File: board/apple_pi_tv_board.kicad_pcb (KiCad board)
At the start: 4 copper layers, 61 x 85.1 mm, 78 parts, among them J1 RJ45, J3 5-1775444-8, J4 JTAG_TC2030, J5 BM02B-ACHSS-GAN-TF, T1 H5007NL, U1 HDMI/USB, U11 TPD4EUSB30, U12 RT9742GGJ5, U2 apple tv tos link, U3 RPi_4, U4 RP2354A, U5 RT9742GGJ5, U6 TPD4EUSB30, U7 IRM-V838M3-C/TR1, U8 74LVC1G07, U9 TPS61232DRC, Y1 ABM8-272-T3

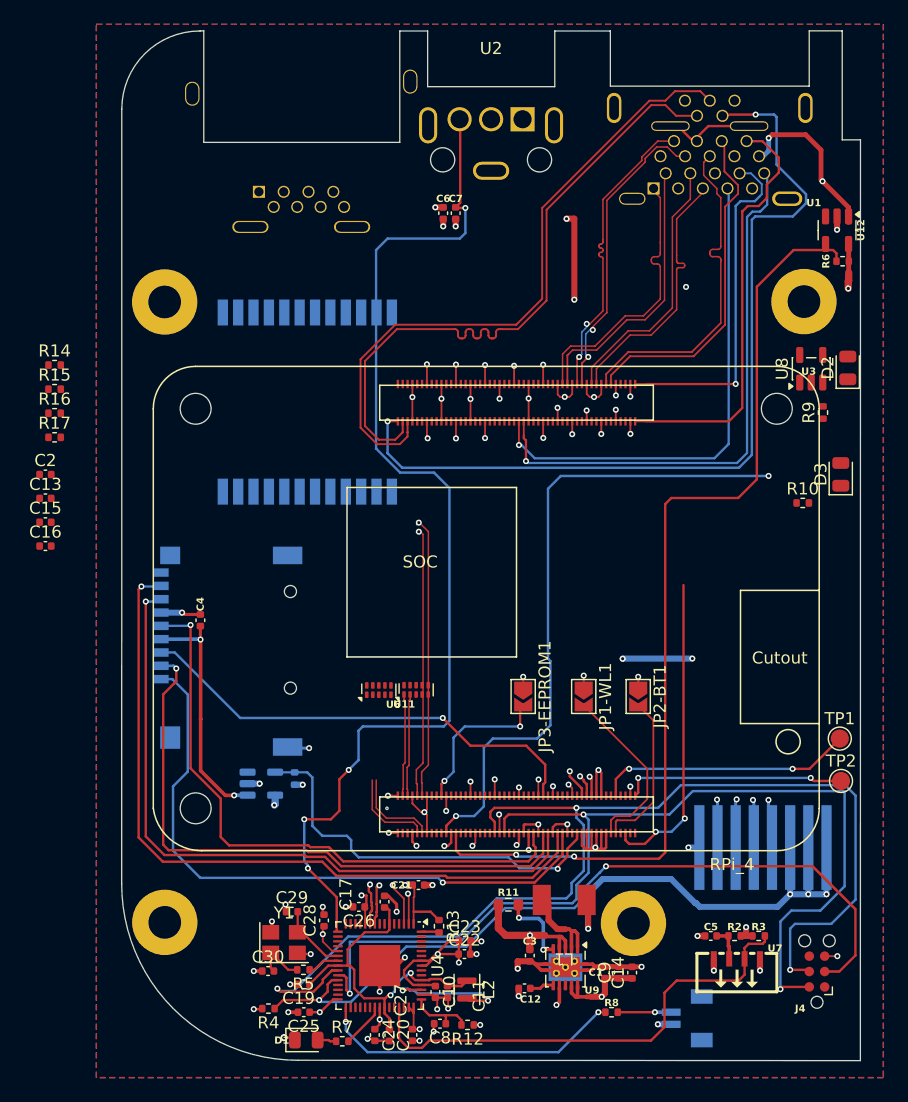
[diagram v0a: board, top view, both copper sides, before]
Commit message: got the ethernet routed
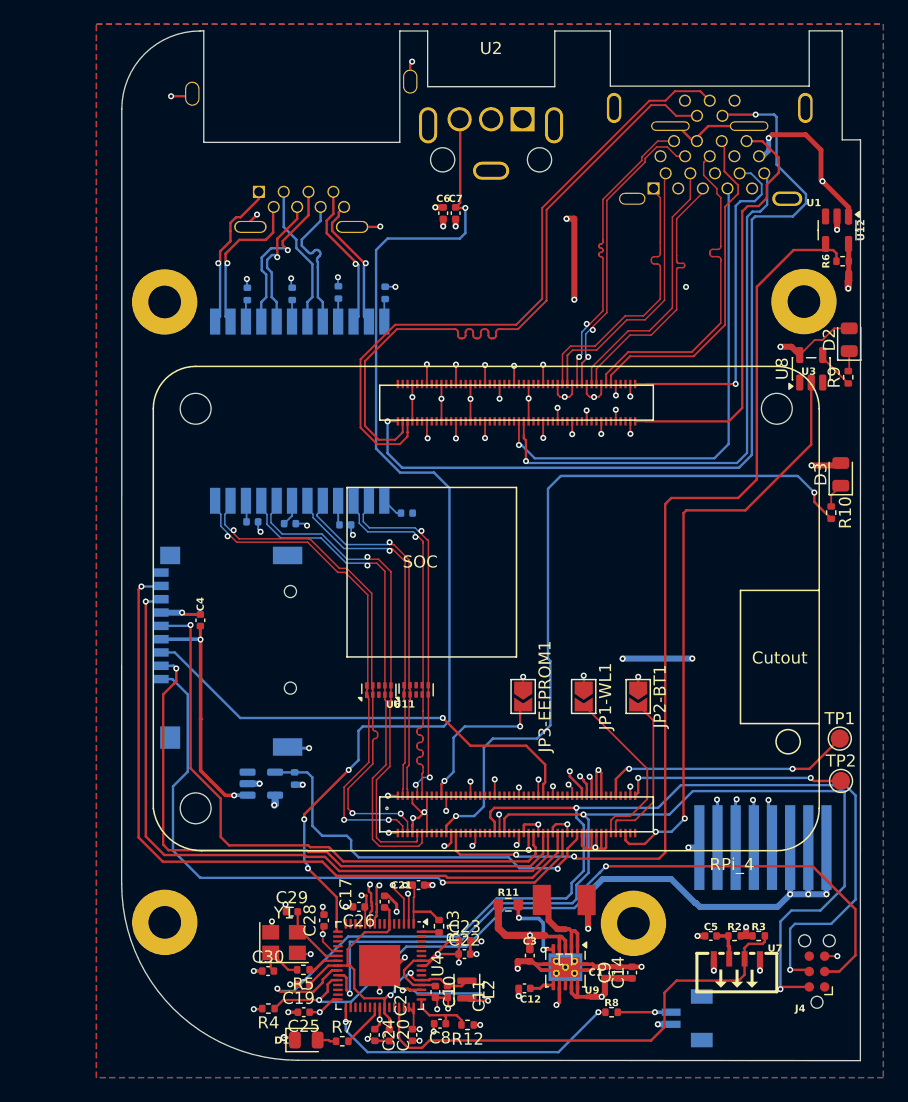
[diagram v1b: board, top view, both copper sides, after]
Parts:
- C13, C15, C16, C2: value C_Small -> 0.1uf; moved to B.Cu
- J1: value RJ45 -> RJ45_Shielded
- R14, R15, R16, R17: moved to B.Cu
- moved C16 30.0 mm to (101.6, 105.4), turned to 180 degrees
- moved R14 27.9 mm to (99.8, 87.2), turned to -90 degrees
- moved C2 25.1 mm to (96.6, 106.3), turned to 180 degrees
- moved R15 24.8 mm to (96.0, 87.2), turned to -90 degrees
- moved R16 22.0 mm to (92.2, 87.3), turned to -90 degrees
- moved C13 20.3 mm to (92.0, 106.2), turned to 180 degrees
- moved R17 19.8 mm to (88.5, 87.3), turned to -90 degrees
- moved C15 17.1 mm to (88.9, 106.1), turned to 180 degrees
- moved R9 3.58 mm to (138.1, 94.2)
- moved R10 2.48 mm to (136.7, 105.3), turned to -90 degrees
- moved D2 2.33 mm to (138.2, 91.1)
- moved T1 0.98 mm to (92.8, 97.0)
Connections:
- J1 pad 1: unconnected-(J1-Pad1) -> /HDMI_RJ45_USB/MX3_P
- J1 pad 2: unconnected-(J1-Pad2) -> /HDMI_RJ45_USB/MX3_N
- J1 pad 3: unconnected-(J1-Pad3) -> /HDMI_RJ45_USB/MX1_P
- J1 pad 4: unconnected-(J1-Pad4) -> /HDMI_RJ45_USB/MX2_N
- J1 pad 5: unconnected-(J1-Pad5) -> /HDMI_RJ45_USB/MX2_P
- J1 pad 6: unconnected-(J1-Pad6) -> /HDMI_RJ45_USB/MX1_N
- J1 pad 7: unconnected-(J1-Pad7) -> /HDMI_RJ45_USB/MX0_P
- J1 pad 8: unconnected-(J1-Pad8) -> /HDMI_RJ45_USB/MX0_N
- U11 pad 4: unconnected-(U11-D2+-Pad4) -> /TRD0_P
- U11 pad 5: unconnected-(U11-D2--Pad5) -> /TRD0_N
- U6 pad 1: /TRD3_N -> /TRD3_P
- U6 pad 2: /TRD3_P -> /TRD3_N
- U6 pad 4: /TRD2_N -> /TRD2_P
- U6 pad 5: /TRD2_P -> /TRD2_N
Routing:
- net /TRD3_N: track 0.00 -> 42.3 mm, vias 0 -> 3
- net /TRD3_P: track 0.00 -> 42.1 mm, vias 0 -> 3
- net /TRD2_P: track 7.29 -> 41.5 mm, vias 0 -> 1
- net /TRD2_N: track 7.30 -> 40.4 mm, vias 0 -> 1
- net +3V3: track 182.7 -> 208.6 mm, vias 20 -> 22
- net Net-(U3A-PI_LED_~{PWR}): track 25.9 -> 49.8 mm
- net /TRD1_P: track 8.48 -> 30.3 mm, vias 0 -> 1
- net /TRD1_N: track 8.48 -> 30.3 mm, vias 0 -> 1
- net GND: track 147.7 -> 162.0 mm, vias 84 -> 95
- net /HDMI_RJ45_USB/MX2_P: track 0.00 -> 14.0 mm, vias 0 -> 1
- net /HDMI_RJ45_USB/MX3_N: track 0.00 -> 12.7 mm, vias 0 -> 1
- net /HDMI_RJ45_USB/MX3_P: track 0.00 -> 12.6 mm, vias 0 -> 1
- net /HDMI_RJ45_USB/MX0_P: track 0.00 -> 12.3 mm, vias 0 -> 1
- net /HDMI_RJ45_USB/MX1_P: track 0.00 -> 11.9 mm
- net /HDMI_RJ45_USB/MX1_N: track 0.00 -> 11.8 mm
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
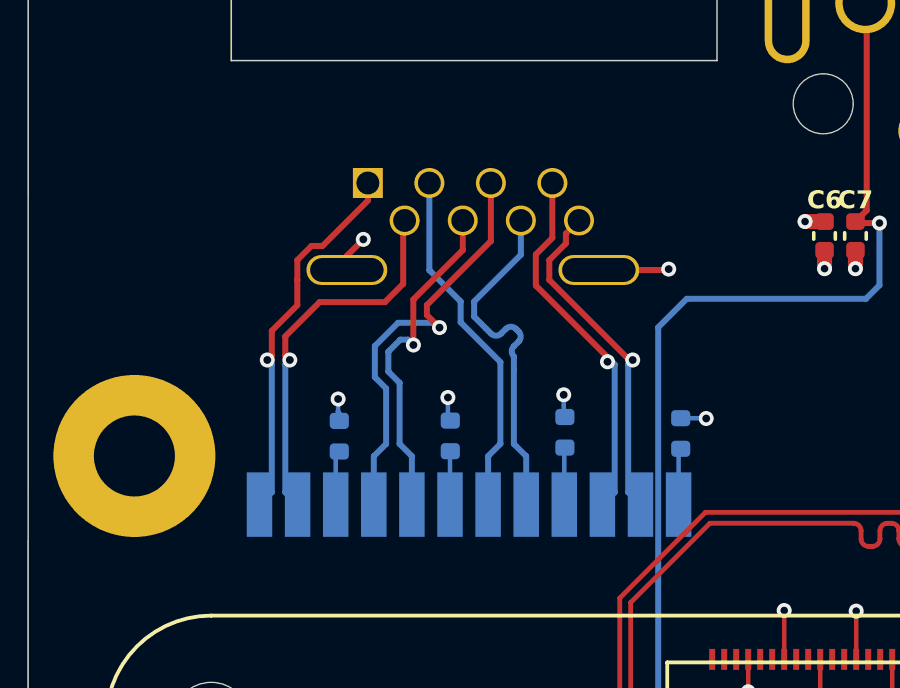
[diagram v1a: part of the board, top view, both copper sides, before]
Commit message: removed some via's
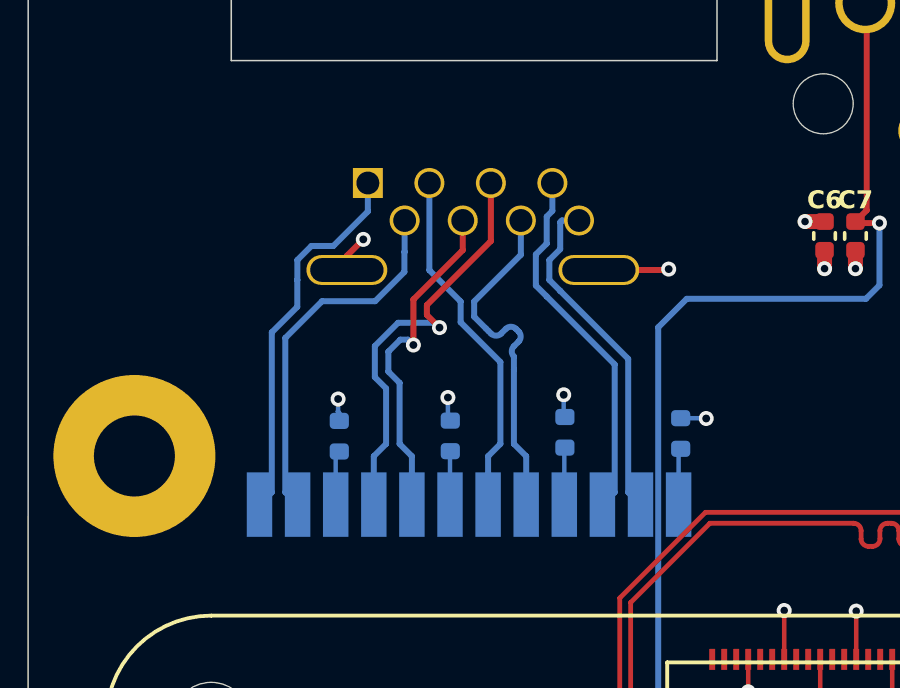
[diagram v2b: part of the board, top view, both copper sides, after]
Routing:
- net /HDMI_RJ45_USB/MX3_N: track 12.7 -> 12.4 mm, vias 1 -> 0
- net /HDMI_RJ45_USB/MX0_N: track 11.3 -> 11.5 mm, vias 1 -> 0
- net /HDMI_RJ45_USB/MX0_P: track 12.3 -> 12.2 mm, vias 1 -> 0
- net /HDMI_RJ45_USB/MX3_P: track 12.6 -> 12.7 mm, vias 1 -> 0

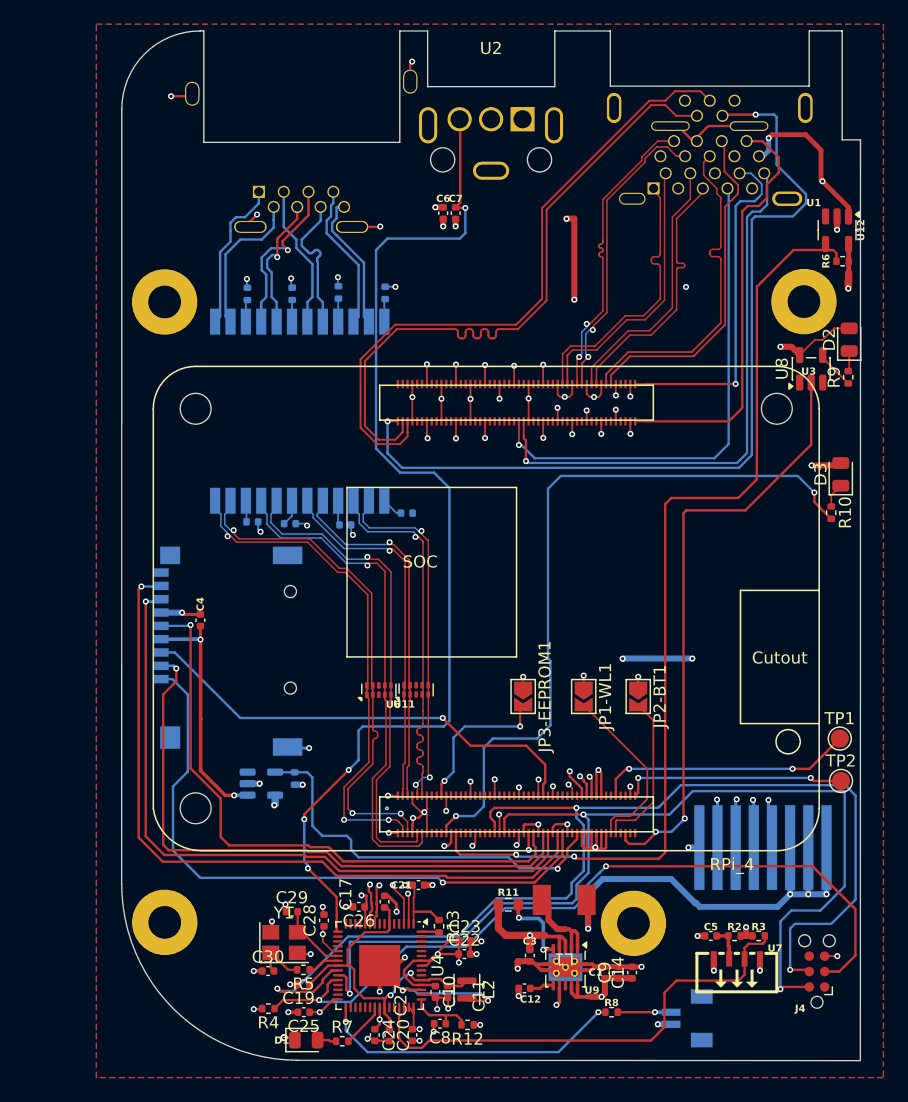
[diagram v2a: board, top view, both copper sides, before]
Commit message: made the cutout for the magnet isolater
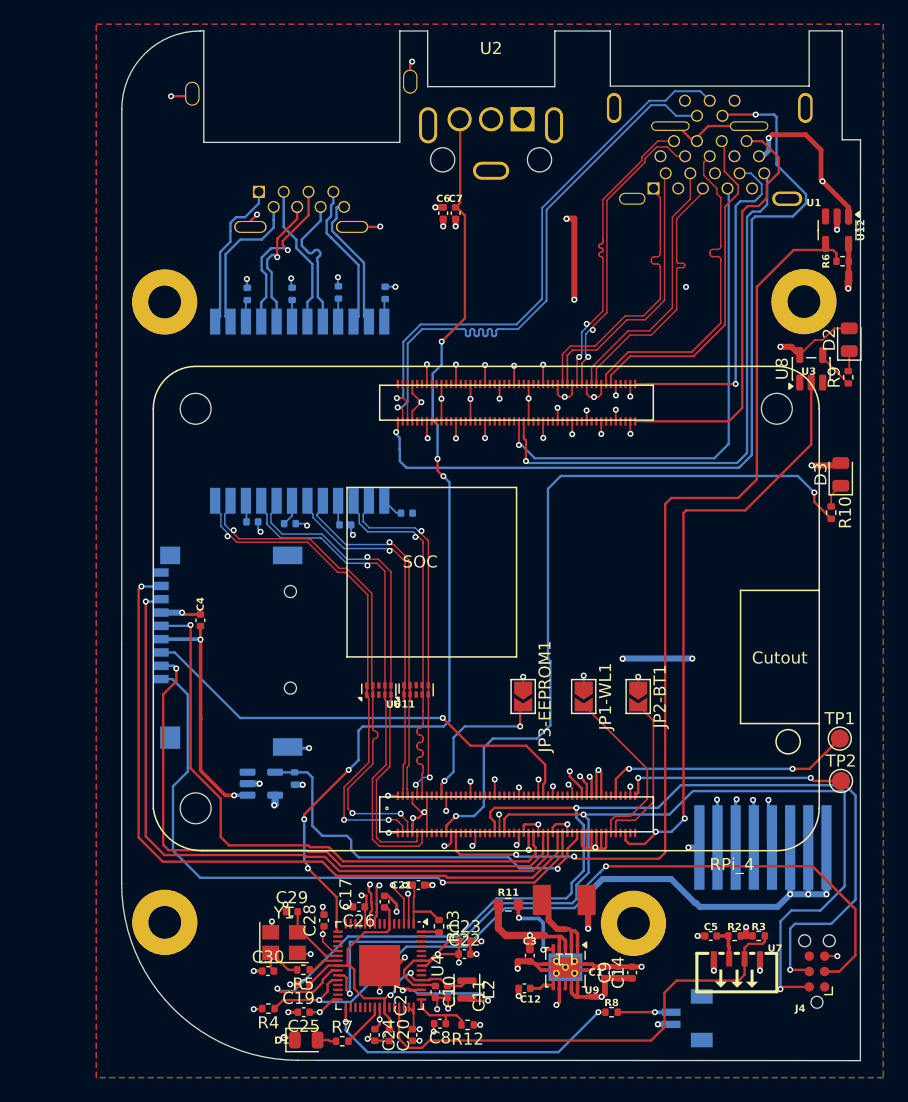
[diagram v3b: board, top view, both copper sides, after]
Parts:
- R10, R9: value R -> 1k
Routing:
- net /Pico_TOSLINK_IR/toslink: track 88.0 -> 78.6 mm, vias 4 -> 6
- net /USB_D+: track 54.4 -> 46.3 mm, vias 0 -> 1
- net /USB_D-: track 54.3 -> 47.7 mm, vias 0 -> 1
- net /USB_ID: track 71.5 -> 70.2 mm
- net GND: track 162.0 -> 162.6 mm

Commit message: should be the last build
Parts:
- moved J3 3.08 mm to (131.0, 134.5), turned to 180 degrees
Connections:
- J3 pad 1: GND -> /Power/power in
- J3 pad 2: GND -> /Power/power in
- J3 pad 3: GND -> /Power/power in
- J3 pad 6: /Power/power in -> GND
- J3 pad 7: /Power/power in -> GND
- J3 pad 8: /Power/power in -> GND
